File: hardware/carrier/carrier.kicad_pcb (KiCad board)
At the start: 4 copper layers, 165 x 103 mm, 157 parts, among them J1 Harness_4Runner, J2 Pi 4 GPIO, J3 UART, M1 FAN1, M2 FAN2, Q1 BUK7Y4R8-60E, Q2 BUK7Y4R8-60E, Q3 MMBT3904, Q4 MMBT3904, Q5 MMBT3904, Q6 2N7002, Q7 2N7002, U1 LM74800-Q1, U2 ADS1115IDGS, U3 DS3231SN, U4 CAT24C32, U5 LM61460-Q1, U6 TLV75533PDBV, U7 TAS6424E-Q1, U8 PCM1808-Q1, X1 12.288MHz

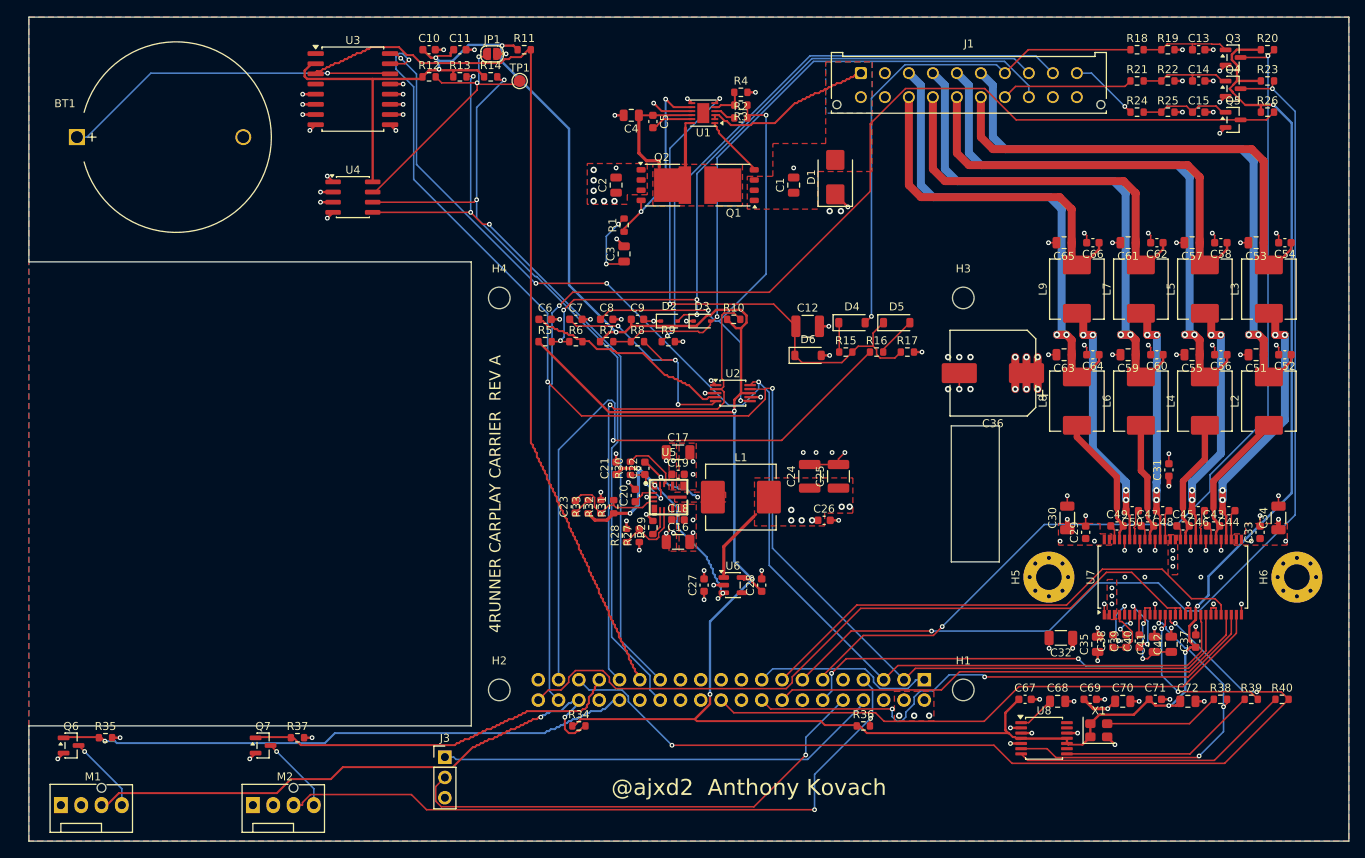
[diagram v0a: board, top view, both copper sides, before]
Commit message: Carrier: route with the mic and LEDs, outline from real measurements
Measured on the screen (Pi edge to screen edge: 36.65 / 43.40 / 15.35 /
31.45 mm): the outline moves 1.35 mm toward the ports; parts stay. The
clock-parts row and the mic jack pulled in to keep copper 3 mm from the
edges. DRC: 0 errors, 0 unrouted.

Build: a repair pass deletes autorouted tracks that DRC flags as shorts
or clearance errors and re-routes those links; CBOOT, EN/SYNC and
I2S_FSYNC are pre-routed. CBOOT is placed by hand (its escape is off the
router's grid). Fit plate regenerated with the corrected outline.

Co-Authored-By: Claude Opus 5.5 <noreply@anthropic.com>
Claude-Session: https://claude.ai/code/session_01EoLoLi7g91W5u4w3UzwQgu
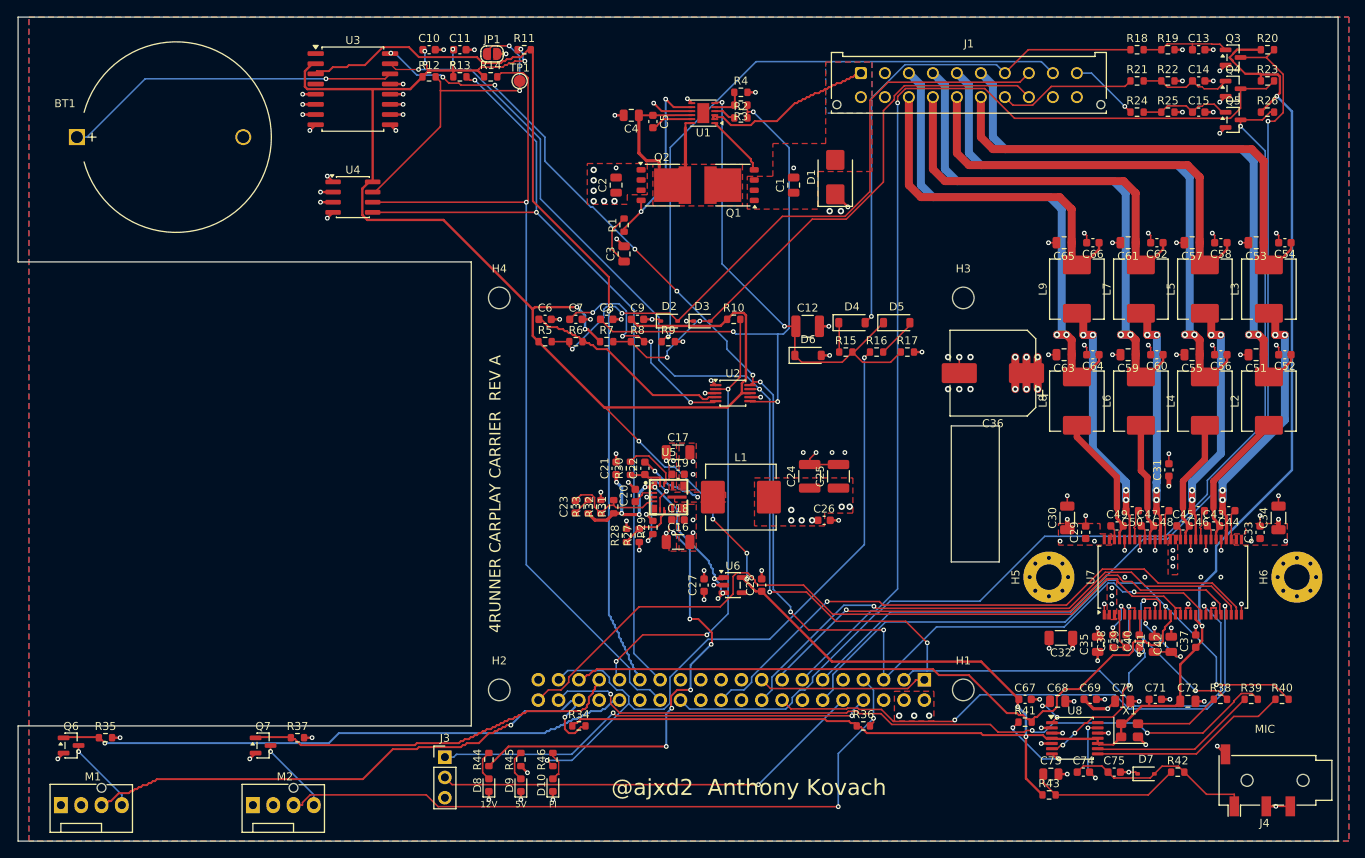
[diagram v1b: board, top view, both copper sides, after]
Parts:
- added C73: 10uF, Capacitor_SMD:C_0805_2012Metric, F.Cu at (227.7, 194.6)
- added C74: 1uF, Capacitor_SMD:C_0603_1608Metric, F.Cu at (231.8, 194.4)
- added C75: 1nF, Capacitor_SMD:C_0603_1608Metric, F.Cu at (235.7, 194.4)
- added D10: RED, LED_SMD:LED_0603_1608Metric, F.Cu at (165.5, 196.0)
- added D7: H15VND3B, Diode_SMD:D_SOD-323, F.Cu at (239.6, 194.6)
- added D8: RED, LED_SMD:LED_0603_1608Metric, F.Cu at (157.5, 196.0)
- added D9: RED, LED_SMD:LED_0603_1608Metric, F.Cu at (161.5, 196.0)
- added J4: MIC, Connector_Audio:Jack_3.5mm_PJ320D_Horizontal, F.Cu at (254.5, 195.4)
- added R41: 33R, Resistor_SMD:R_0603_1608Metric, F.Cu at (224.5, 188.1)
- added R42: 2.2k, Resistor_SMD:R_0603_1608Metric, F.Cu at (243.6, 194.4)
- added R43: 1k, Resistor_SMD:R_0603_1608Metric, F.Cu at (227.5, 197.2)
- added R44: 10k, Resistor_SMD:R_0603_1608Metric, F.Cu at (157.5, 192.8)
- added R45: 1k, Resistor_SMD:R_0603_1608Metric, F.Cu at (161.5, 192.8)
- added R46: 1k, Resistor_SMD:R_0603_1608Metric, F.Cu at (165.5, 192.8)
- moved U8 3.85 mm to (230.7, 190.1)
- moved X1 3.85 mm to (237.6, 189.1)
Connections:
- J2 pad 26: unconnected-(J2-GPIO7-Pad26) -> /~{REVERSE}
- J2 pad 38: /~{REVERSE} -> /I2S_DIN
- R39 pad 1: Net-(U8-BCK) -> Net-(U8-DOUT)
- R39 pad 2: /I2S_BCLK -> /I2S_DIN
- R40 pad 1: Net-(U8-LRCK) -> Net-(U8-BCK)
- R40 pad 2: /I2S_FSYNC -> /I2S_BCLK
- U8 pad 13: unconnected-(U8-VINL-Pad13) -> /MIC_IN
- U8 pad 9: unconnected-(U8-DOUT-Pad9) -> Net-(U8-DOUT)
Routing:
- net /I2S_DIN: track 0.00 -> 94.5 mm, vias 0 -> 3
- net +12V_PROT: track 24.4 -> 80.3 mm, vias 33 -> 38
- net /I2S_FSYNC: track 116.4 -> 86.1 mm, vias 3 -> 0
- net +3V3: track 400.2 -> 427.2 mm, vias 11 -> 16
- net Net-(U8-LRCK): track 35.3 -> 9.73 mm, vias 0 -> 2
- net /MIC_T: track 0.00 -> 24.1 mm
- net /~{REVERSE}: track 157.8 -> 133.9 mm
- net Net-(U8-DOUT): track 0.00 -> 21.0 mm
- net Net-(C73-Pad1): track 0.00 -> 18.9 mm
- net /SYS_EN: track 68.9 -> 57.9 mm
- net GND: track 134.1 -> 145.0 mm, vias 125 -> 132
- net /PI_HOLD: track 79.9 -> 90.5 mm, vias 1 -> 2
- net Net-(U5-RT): track 3.40 -> 13.6 mm, vias 0 -> 2
- net /~{AMP_MUTE}: track 61.4 -> 71.4 mm, vias 0 -> 2
- net /MIC_IN: track 0.00 -> 8.90 mm, vias 0 -> 2
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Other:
- outline, holes or cut-outs redrawn
- board text added: "12V"
- board text added: "5V"
- board text added: "MIC"
- board text added: "PI"

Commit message: Carrier: outline from the manufacturer's drawing (164.9 x 102.0)
The Hosyond drawing confirms the measured Pi position within 0.2 mm and
gives the exact screen size; the outline is trimmed to match (it
overhung the bottom by ~1.1 mm). Edge margin 2.5 mm now the Pi position
is settled. DRC: 0 errors, 0 unrouted. The screen's corner holes are
for the enclosure; no board change.

Co-Authored-By: Claude Opus 5.5 <noreply@anthropic.com>
Claude-Session: https://claude.ai/code/session_01EoLoLi7g91W5u4w3UzwQgu
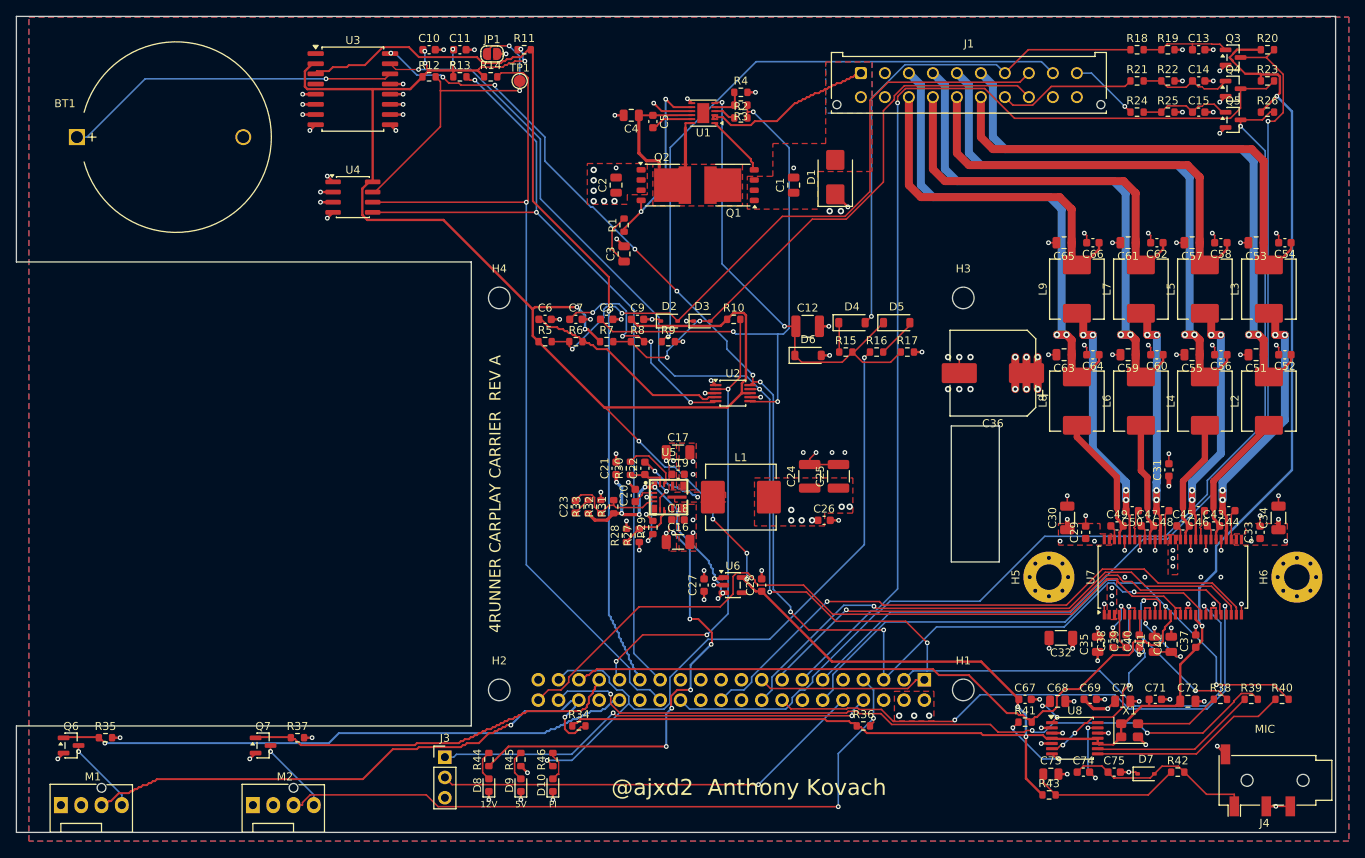
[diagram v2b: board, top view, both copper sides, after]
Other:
- board size 165 x 103 mm -> 164.9 x 102 mm
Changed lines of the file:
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@@
 	)
 	(gr_line
-		(start 98.65 100)
-		(end 263.649999 100)
+		(start 98.44 99.91)
+		(end 263.34 99.91)
 		(stroke
 			(width 0.1)
@@
 	)
 	(gr_line
-		(start 98.65 130.6)
-		(end 98.65 100)
+		(start 98.44 130.6)
+		(end 98.44 99.91)
 		(stroke
 			(width 0.1)
@@
 	)
 	(gr_line
-		(start 98.65 188.6)
+		(start 98.44 188.6)
 		(end 155.3 188.6)
 		(stroke
@@
 	)
 	(gr_line
-		(start 98.65 203)
-		(end 98.65 188.6)
+		(start 98.44 201.91)
+		(end 98.44 188.6)
 		(stroke
 			(width 0.1)
@@
 	(gr_line
 		(start 155.3 130.6)
-		(end 98.65 130.6)
+		(end 98.44 130.6)
 		(stroke
 			(width 0.1)
@@
 	)
 	(gr_line
-		(start 263.649999 100)
-		(end 263.649999 203)
+		(start 263.34 99.91)
+		(end 263.34 201.91)
 		(stroke
 			(width 0.1)
@@
 	)
 	(gr_line
-		(start 263.649999 203)
-		(end 98.65 203)
+		(start 263.34 201.91)
+		(end 98.44 201.91)
 		(stroke
 			(width 0.1)
@@
 		(locked yes)
 		(layers "F.Cu" "B.Cu" "In1.Cu" "In2.Cu")
+		(name "edge right")
+		(hatch edge 0.5)
+		(connect_pads
+			(clearance 0)
+		)
+		(min_thickness 0.25)
+		(keepout
+			(tracks not_allowed)
+			(vias not_allowed)
+			(pads allowed)
+			(copperpour not_allowed)
+			(footprints allowed)
+		)
+		(placement
+			(enabled no)
+			(sheetname "")
+		)
+		(fill
+			(thermal_gap 0.5)
+			(thermal_bridge_width 0.5)
+			(island_removal_mode 0)
+		)
+		(polygon
+			(pts
+				(xy 260.84 98.91) (xy 264.34 98.91) (xy 264.34 202.91) (xy 260.84 202.91)
+			)
+		)
+	)
+	(zone
+		(locked yes)
+		(layers "F.Cu" "B.Cu" "In1.Cu" "In2.Cu")
 		(name "edge bottom")
 		(hatch edge 0.5)
@@
 		(polygon
 			(pts
-				(xy 97.65 200) (xy 264.649999 200) (xy 264.649999 204) (xy 97.65 204)
+				(xy 97.44 199.41) (xy 264.34 199.41) (xy 264.34 202.91) (xy 97.44 202.91)
+			)
+		)
+	)
+	(zone
+		(locked yes)
+		(layers "F.Cu" "B.Cu" "In1.Cu" "In2.Cu")
+		(name "slot band")
+		(hatch edge 0.5)
+		(connect_pads
+			(clearance 0)
+		)
+		(min_thickness 0.25)
+		(keepout
+			(tracks not_allowed)
+			(vias not_allowed)
+			(pads allowed)
+			(copperpour not_allowed)
+			(footprints allowed)
+		)
+		(placement
+			(enabled no)
+			(sheetname "")
+		)
+		(fill
+			(thermal_gap 0.5)
+			(thermal_bridge_width 0.5)
+			(island_removal_mode 0)
+		)
+		(polygon
+			(pts
+				(xy 214.8 150.6) (xy 221.8 150.6) (xy 221.8 168.6) (xy 214.8 168.6)
 			)
 		)
@@
 		(polygon
 			(pts
-				(xy 97.65 99) (xy 264.649999 99) (xy 264.649999 103) (xy 97.65 103)
+				(xy 97.44 98.91) (xy 264.34 98.91) (xy 264.34 102.41) (xy 97.44 102.41)
+			)
+		)
+	)
+	(zone
+		(locked yes)
+		(layers "F.Cu" "B.Cu" "In1.Cu" "In2.Cu")
+		(name "edge left")
+		(hatch edge 0.5)
+		(connect_pads
+			(clearance 0)
+		)
+		(min_thickness 0.25)
+		(keepout
+			(tracks not_allowed)
+			(vias not_allowed)
+			(pads allowed)
+			(copperpour not_allowed)
+			(footprints allowed)
+		)
+		(placement
+			(enabled no)
+			(sheetname "")
+		)
+		(fill
+			(thermal_gap 0.5)
+			(thermal_bridge_width 0.5)
+			(island_removal_mode 0)
+		)
+		(polygon
+			(pts
+				(xy 97.44 98.91) (xy 100.94 98.91) (xy 100.94 202.91) (xy 97.44 202.91)
+			)
+		)
+	)
+	(zone
+		(locked yes)
+		(layers "F.Cu" "B.Cu" "In1.Cu" "In2.Cu")
+		(name "notch band")
+		(hatch edge 0.5)
+		(connect_pads
+			(clearance 0)
+		)
+		(min_thickness 0.25)
+		(keepout
+			(tracks not_allowed)
+			(vias not_allowed)
+			(pads allowed)
+			(copperpour not_allowed)
+			(footprints allowed)
+		)
+		(placement
+			(enabled no)
+			(sheetname "")
+		)
+		(fill
+			(thermal_gap 0.5)
+			(thermal_bridge_width 0.5)
+			(island_removal_mode 0)
+		)
+		(polygon
+			(pts
+				(xy 99 130.1) (xy 155.8 130.1) (xy 155.8 189.1) (xy 99 189.1)
 			)
 		)
@@
 		(locked yes)
 		(layers "F.Cu" "B.Cu" "In1.Cu" "In2.Cu")
-		(name "edge right")
+		(name "slot band")
 		(hatch edge 0.5)
 		(connect_pads
@@
 		(polygon
 			(pts
-				(xy 260.649999 99) (xy 264.649999 99) (xy 264.649999 204) (xy 260.649999 204)
+				(xy 214.8 150.6) (xy 221.8 150.6) (xy 221.8 168.6) (xy 214.8 168.6)
 			)
 		)
@@
 		(locked yes)
 		(layers "F.Cu" "B.Cu" "In1.Cu" "In2.Cu")
-		(name "edge left")
+		(name "notch band")
 		(hatch edge 0.5)
 		(connect_pads
@@
 		(polygon
 			(pts
-				(xy 97.65 99) (xy 101.65 99) (xy 101.65 204) (xy 97.65 204)
+				(xy 99 130.1) (xy 155.8 130.1) (xy 155.8 189.1) (xy 99 189.1)
 			)
 		)

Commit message: Carrier: silkscreen tidy, harness pin table, JLCPCB order files
Labels 0.8 mm, hidden where they clash with pads, labels or the edge
(JLC places from the CPL). Harness pin table on the underside by J1.
tools/jlc_export.sh writes fab/: Gerbers + drill zip, BOM (no ref
ranges) and CPL; all 162 parts match between them.

Co-Authored-By: Claude Opus 5.5 <noreply@anthropic.com>
Claude-Session: https://claude.ai/code/session_01EoLoLi7g91W5u4w3UzwQgu
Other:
- board text added: "J1 HARNESS (pin n sits above n+10) 1/11 +12V BATT 2/12/19 GND 3/13 FR +/- 4/14 FL +/- 5/15 RR +/- 6/16 RL +/- 7 ACC 17 ILLUM 10 REVERSE 8 SWC1 18 SWC2 9 SWC GND"
